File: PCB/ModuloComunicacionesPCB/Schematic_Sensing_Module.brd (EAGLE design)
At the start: 160 x 100 mm, 73 parts, among them J1 TERMINAL-TB3, J2 TERMINAL-TB3, J3 TERMINAL-TB3, J4 TERMINAL-TB3, Q1 CSM-7X-DU, Q2 MMBT2222A, SW2 1825910-6, U1 ATMEGA328P-PU, U2 LP38692MP-5.0, U3 MCP1501T-18E/SN, U4 ACS723LLCTR-05AB-T, U5 OPA320AIDBVR

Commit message: avances en placing de la pcb del transmisor
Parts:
- removed BAT_PIN: (no value), pinhead:1X02
- removed C24: (no value), rcl:C0805
- removed FTDI_PIN: (no value), pinhead:1X04
- removed J1, J2, J3, J4: TERMINAL-TB3, TERMINAL-TB001:TERMINAL-TB3
- removed Q2: MMBT2222A, MMBT2222A:SOT23
- removed R15, R16, R17, R3, R4, R5: 0.1, rcl:R1206
- removed U$2, U$7: REF3450, SOT95P280X145-6N:SOT95P280X145-6N
- removed U$3: MCP6002-E/MS, MCP6002-E_MS:SOP65P490X110-8N
- removed U$6: TERMINAL-TB2, TERMINAL-TB001:TERMINAL-TB2
- removed U2: LP38692MP-5.0, LP38692MP-5.0:SOT150P696X180-5N
- removed U4: ACS723LLCTR-05AB-T, ACS723LLCTR-05AB-T:SOIC127P600X175-8N
- removed U5: OPA320AIDBVR, OPA320AIDBVR:SOT95P280X145-5N
- added 2N2222: MMBT2222A, MMBT2222A:SOT23
- added ACS723: ACS723LLCTR-05AB-T, ACS723LLCTR-05AB-T:SOIC127P600X175-8N
- added C29, C30, C31, C32: 0.1uF, rcl:C1206
- added C33: 1nF, rcl:C1206
- added C34, C35: 2.2uF, rcl:C1206
- added IACT: (no value), TERMINAL-TB001:TERMINAL-TB2
- added JP1: (no value), pinhead:1X04/90
- added LP38692: LP38692MP-5.0, LP38692MP-5.0:SOT150P696X180-5N
- added MCP6002: MCP6002-E/MS, MCP6002-E_MS:SOP65P490X110-8N
- added OPA320: OPA320AIDBVR, OPA320AIDBVR:SOT95P280X145-5N
- added R3450, REF3450: REF3450, SOT95P280X145-6N:SOT95P280X145-6N
- added TS1, TS2, WS1, WS2: (no value), TERMINAL-TB001:TERMINAL-TB3
- C11, C12: value 22p -> 22pF; device rcl:C1206 -> rcl:C0805
- C14, C15, C20, C21: value 100n -> 100nF
- C17: value 8.2pF -> 18pF
- C2, C3: value 1uF -> cambiar por los de 10uF ceramicos de didacticas
- C22: value 0.1u -> 0.1uF
- C25, C26, C27, C28: value 0.1nF -> 0.1uF
- U$4: value INA219_BB -> INABB; device INA219_BB:INA219_BB -> INA219BB:INA219-MODULE
- moved C27 315.3 mm to (98.1, 114.0)
- moved C28 309.0 mm to (80.7, 116.0)
- moved C22 235.1 mm to (151.1, 114.0)
- moved C25 210.0 mm to (60.2, 23.8), turned to 180 degrees
- moved U$8 208.7 mm to (83.3, 59.1), turned to 270 degrees
- moved R19 205.8 mm to (60.1, 18.4), turned to 180 degrees
- moved LED4 199.4 mm to (115.7, 74.0), turned to 90 degrees
- moved C26 196.9 mm to (46.2, 17.6), turned to 270 degrees
- moved LED3 195.6 mm to (116.1, 66.9), turned to 270 degrees
- moved R1 192.7 mm to (90.5, 38.5), turned to 180 degrees
- moved R12 191.1 mm to (98.1, 106.3)
- moved R7 189.3 mm to (107.7, 67.0), turned to 180 degrees
- moved SW2 187.5 mm to (115.8, 57.7), turned to 90 degrees
- moved R18 186.2 mm to (41.4, 17.6), turned to 270 degrees
- moved C23 170.4 mm to (66.0, 38.5)
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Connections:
- removed net +5V: U$1.IN+
- removed net A0: U1.23
- removed net A1: U1.24
- removed net A2: U1.25
- removed net A3: U1.26
- removed net N$1: R3.2, U$2.1
- removed net N$10: U$6.1, U4.1, U4.2
- removed net N$11: U$6.2, U4.3, U4.4
- removed net N$12: R11.2, U4.7
- removed net N$13: C9.1, R12.2, U5.3
- removed net N$15: C10.1, R13.1, U5.1, U5.4
- removed net N$18: R16.2, U$7.6
- removed net N$19: R17.2, U$7.5
- removed net N$20: R15.2, U$7.1
- removed net N$24: C25.1, R19.1, U$3.3
- removed net N$25: C26.1, R18.1, U$3.5
- removed net N$5: R4.2, U$2.6
- removed net N$6: R5.2, U$2.5
- removed net N$8: R10.1, U4.6
- removed net VOUT-: U$1.VOUT-
- new net BWSEL: ACS723.6, R10.1
- new net IP+: ACS723.1, ACS723.2, IACT.1
- new net IP-: ACS723.3, ACS723.4, IACT.2
- new net VIN+: C9.1, OPA320.3, R12.2
- new net VIN-: C10.1, OPA320.1, OPA320.4, R13.1
- new net VO: ACS723.7, C33.1, R11.2
- net B+INA: now also U$4.6
- net B-INA: now also U$4.5; no longer BAT_PIN.1
- net BATL: now also U1.13; no longer U1.11
- net DATAT1: now also TS1.2, U1.14; no longer J3.2
- net DATAT2: now also TS2.2, U1.15; no longer J4.2
- net DATAW1: now also C25.1, MCP6002.3, R19.1, WS1.3; no longer J1.3
- net DATAW2: now also C26.1, MCP6002.5, R18.1, WS2.3; no longer J2.3
- net DTR: now also JP1.4; no longer FTDI_PIN.4
- net GND: now also ACS723.5, C29.2, C30.2, C31.2, C32.2, C33.2, C34.1, C35.2, JP1.1, LP38692.5, MCP6002.4, OPA320.2, R3450.1, R3450.2, REF3450.1, REF3450.2, TS1.3, TS2.3, U$1.VOUT-, U$4.2, U$8.DIO0, U$8.DIO1, U$8.DIO2, U$8.DIO3, U$8.DIO4, U1.25, U1.26, U1.6, WS1.1, WS2.1; no longer BAT_PIN.2, C24.2, FTDI_PIN.1, J1.1, J2.1, J3.3, J4.3, R15.1, R3.1, U$2.2, U$3.4, U$7.2, U2.5, U4.5, U5.2
- net N$2: now also 2N2222.1; no longer Q2.1
- net OSC+: now also C12.1; no longer C11.1
- net OSC-: now also C11.1; no longer C12.1
- net RX0: now also JP1.3; no longer FTDI_PIN.3
- net RX1: now also U$8.TX
- net SCL: now also U$4.3
- net SDA: now also U$4.4
- net TX0: now also JP1.2; no longer FTDI_PIN.2
- net TX1: now also U$8.RX
- net VACS: now also ACS723.8, REF3450.5, REF3450.6; no longer R16.1, R17.1, U4.8
- net VDD33: now also C29.1, U$4.1; no longer C17.1, C24.1
- net VLP5: now also C30.1, C31.1, C32.1, C34.2, LP38692.3, MCP6002.8, TS1.1, TS2.1, U1.21, WS1.2, WS2.2; no longer J1.2, J2.2, J3.1, J4.1, U$3.8, U2.3
- net VOREG: now also 2N2222.2, R3450.3, R3450.4, REF3450.3, REF3450.4; no longer Q2.2, U$2.3, U$2.4, U$7.3, U$7.4
- net VOUT+: now also C17.1, C35.1
- net VOW1: now also MCP6002.1, MCP6002.2, U1.23; no longer U$3.1, U$3.2
- net VOW2: now also MCP6002.6, MCP6002.7, U1.24; no longer U$3.6, U$3.7
- net VREF5: now also OPA320.5, R3450.5, R3450.6; no longer R4.1, R5.1, U5.5
- net VSUPPLY: now also 2N2222.3, LP38692.1, LP38692.4; no longer Q2.3, U2.1, U2.4

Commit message: placing almost done
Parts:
- removed C34: 2.2uF, rcl:C1206
- removed JP1: (no value), pinhead:1X04/90
- removed LED3, LED4: (no value), led:CHIPLED_1206
- removed U$4: INABB, INA219BB:INA219-MODULE
- removed U$5: MCP33121, mcp33121:MSOP10
- removed U1: ATMEGA328P-PU, Atmel_By_element14_Batch_1-00:DIP254P762X457-28
- removed U3: MCP1501T-18E/SN, MCP1501T-18E_SN:SOIC127P600X175-8N
- added ATMEGA328P: ATMEGA328P-PU, Atmel_By_element14_Batch_1-00:DIP254P762X457-28
- added BAT+, BAT-: (no value), led:CHIPLED_1206
- added INA219: INABB, INA219BB:INA219-MODULE
- added JP2: (no value), pinhead:1X04
- added MCP18: MCP1501T-18E/SN, MCP1501T-18E_SN:SOIC127P600X175-8N
- added MCP33121: MCP33121, mcp33121:MSOP10
- added TS3: (no value), TERMINAL-TB001:TERMINAL-TB3
- C18: value 1uF -> 0.1uF
- C19: value 10uF -> 0.1uF
- moved R9 144.9 mm to (28.8, 12.7)
- moved R6 126.5 mm to (28.6, 20.9)
- moved C32 125.6 mm to (129.2, 24.3), turned to 180 degrees
- moved R11 118.6 mm to (111.6, 40.0)
- moved R14 117.9 mm to (99.1, 44.0), turned to 180 degrees
- moved R13 115.0 mm to (99.5, 40.2), turned to 180 degrees
- moved C20 112.0 mm to (92.6, 32.6), turned to 180 degrees
- moved C8 112.0 mm to (28.9, 16.9)
- moved C16 111.4 mm to (99.2, 32.7)
- moved C19 107.0 mm to (84.2, 24.5), turned to 180 degrees
- moved C31 105.3 mm to (106.1, 24.6), turned to 180 degrees
- moved C7 104.8 mm to (20.0, 22.6)
- moved C15 103.6 mm to (116.1, 32.1), turned to 270 degrees
- moved C21 102.2 mm to (92.5, 44.1)
- moved IACT 101.3 mm to (129.0, 38.4), turned to 90 degrees
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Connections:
- removed net N$16: C13.2, R13.2, U$5.3
- removed net N$17: C13.1, R14.2, U$5.4
- removed net N$7: R6.2, R9.2, U3.7, U3.8
- new net DATAT3: ATMEGA328P.13, C18.1, TS3.2
- new net IN+: C13.2, MCP33121.3, R13.2
- new net IN-: C13.1, MCP33121.4, R14.2
- new net VOMCP18: MCP18.7, MCP18.8, R6.2, R9.2
- net AMISO: now also ATMEGA328P.18, MCP33121.7; no longer U$5.7, U1.18
- net AMOSI: now also ATMEGA328P.17, MCP33121.9; no longer U$5.9, U1.17
- net ASCK: now also ATMEGA328P.19, MCP33121.8; no longer U$5.8, U1.19
- net ASS: now also ATMEGA328P.16, MCP33121.6; no longer U$5.6, U1.16
- net B+INA: now also INA219.6; no longer U$4.6
- net B-INA: now also INA219.5; no longer U$4.5
- net BATH: now also ATMEGA328P.11; no longer U1.12
- net BATL: now also ATMEGA328P.12; no longer U1.13
- net DATAT1: now also ATMEGA328P.14; no longer U1.14
- net DATAT2: now also ATMEGA328P.15; no longer U1.15
- net DTR: now also JP2.4; no longer JP1.4
- net GND: now also ATMEGA328P.22, ATMEGA328P.25, ATMEGA328P.26, ATMEGA328P.6, ATMEGA328P.8, BAT+.C, BAT-.C, C19.2, INA219.2, JP2.1, MCP18.2, MCP18.4, MCP18.5, MCP18.6, MCP33121.5, TS1.1, TS2.1, TS3.1; no longer C19.1, C34.1, JP1.1, LED3.C, LED4.C, TS1.3, TS2.3, U$4.2, U$5.5, U1.22, U1.25, U1.26, U1.6, U1.8, U3.2, U3.4, U3.5, U3.6
- net N$3: now also BAT-.A; no longer LED3.A
- net N$4: now also BAT+.A; no longer LED4.A
- net OSC+: now also ATMEGA328P.9; no longer U1.9
- net OSC-: now also ATMEGA328P.10; no longer U1.10
- net RST: now also ATMEGA328P.1; no longer U1.1
- net RX0: now also ATMEGA328P.2, JP2.3; no longer JP1.3, U1.2
- net RX1: now also ATMEGA328P.4; no longer U1.4
- net SCL: now also ATMEGA328P.28, INA219.3; no longer U$4.3, U1.28
- net SDA: now also ATMEGA328P.27, INA219.4; no longer U$4.4, U1.27
- net TX0: now also ATMEGA328P.3, JP2.2; no longer JP1.2, U1.3
- net TX1: now also ATMEGA328P.5; no longer U1.5
- net VDD33: now also INA219.1; no longer U$4.1
- net VLP5: now also ATMEGA328P.20, ATMEGA328P.21, ATMEGA328P.7, C19.1, MCP33121.10, TS1.3, TS2.3, TS3.3; no longer C19.2, C34.2, TS1.1, TS2.1, U$5.10, U1.20, U1.21, U1.7
- net VOW1: now also ATMEGA328P.23; no longer U1.23
- net VOW2: now also ATMEGA328P.24; no longer U1.24
- net VREF18: now also MCP33121.2; no longer U$5.2
- net VREF5: now also MCP18.1, MCP18.3, MCP33121.1; no longer C18.1, U$5.1, U3.1, U3.3

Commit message: Finished Placing-Give a review
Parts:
- C2, C3: value cambiar por los de 10uF ceramicos de didacticas -> 10uF
- C23, C6: value 1u -> 10u
- moved MCP18 58.4 mm to (54.2, 64.5)
- moved C8 57.1 mm to (60.4, 64.6), turned to 270 degrees
- moved R6 55.7 mm to (63.4, 64.4), turned to 270 degrees
- moved R9 52.8 mm to (54.2, 58.9), turned to 180 degrees
- moved C7 50.1 mm to (47.6, 64.5), turned to 270 degrees
- moved LP38692 43.0 mm to (15.8, 46.9)
- moved C17 41.1 mm to (9.84, 37.7)
- moved C3 37.8 mm to (22.9, 46.3), turned to 90 degrees
- moved C35 36.3 mm to (15.8, 37.8)
- moved D1 30.5 mm to (45.4, 71.6)
- moved JP2 29.4 mm to (53.8, 76.5)
- moved ATMEGA328P 29.4 mm to (57.8, 22.3)
- moved C12 29.2 mm to (46.4, 36.0)
- moved Q1 29.2 mm to (42.0, 33.9)
- moved C11 29.2 mm to (46.4, 31.3)
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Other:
- board size 160 x 100 mm -> 109 x 82 mm

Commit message: pcb ruteada falta plano de tierra
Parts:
- removed JP2: (no value), pinhead:1X04
- removed ON_OFF: (no value), pinhead:1X03
- removed SW2: 1825910-6, button1825910-6:SW_1825910-6-4
- removed TS1, TS2, TS3: (no value), TERMINAL-TB001:TERMINAL-TB3
- removed U$1: MODULO_CARGA_DEVICE, Modulo_Carga:MODULO_CARGA
- added BATPIN: (no value), pinhead:1X02
- added FTDI: (no value), pinhead:1X04
- added JP1, ON/OFF: (no value), pinhead:1X03
- added POWER-SUPP: MODULO_CARGA_DEVICE, Modulo_Carga:MODULO_CARGA
- added RESET: 1825910-6, button1825910-6:SW_1825910-6-4
- added T1, T2, T3: (no value), TERMINAL-TB001:TERMINAL-TB3
- moved BAT- 75.7 mm to (42.9, 4.19), turned to 180 degrees
- moved BAT+ 75.1 mm to (37.8, 5.21), turned to 180 degrees
- moved R7 69.6 mm to (43.0, 11.9)
- moved R8 66.8 mm to (37.9, 11.8), turned to 90 degrees
- moved C29 23.4 mm to (67.7, 58.4), turned to 0 degrees
- moved C21 20.1 mm to (60.2, 18.8), flipped to the bottom, turned to 90 degrees
- moved R14 19.0 mm to (66.9, 19.8)
- moved C2 16.5 mm to (31.8, 52.2)
- moved C23 16.3 mm to (38.8, 64.5)
- moved LP38692 16.0 mm to (31.8, 46.9)
- moved C3 15.9 mm to (38.8, 46.2), turned to 270 degrees
- moved C1 15.8 mm to (45.7, 69.3)
- moved D1 15.2 mm to (60.6, 71.8), turned to 90 degrees
- moved R2 15.0 mm to (38.2, 69.5), turned to 180 degrees
- moved C4 13.4 mm to (22.3, 65.4), turned to 0 degrees
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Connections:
- net N$2 renamed BASE
- removed net AMOSI: ATMEGA328P.17, MCP33121.9
- removed net VO: ACS723.7, C33.1, R11.2
- new net VIN: C33.1, JP1.2, R11.2
- new net VOACS: ACS723.7, JP1.1
- net B+INA: now also POWER-SUPP.BAT+; no longer U$1.BAT+
- net B-INA: now also BATPIN.1
- net DATAT1: now also ATMEGA328P.15, T1.2; no longer ATMEGA328P.14, TS1.2
- net DATAT2: now also ATMEGA328P.13, T2.2; no longer ATMEGA328P.15, TS2.2
- net DATAT3: now also ATMEGA328P.14, T3.2; no longer ATMEGA328P.13, TS3.2
- net DATAW1: now also WS1.2; no longer WS1.3
- net DATAW2: now also WS2.2; no longer WS2.3
- net DTR: now also FTDI.4; no longer JP2.4
- net GND: now also ATMEGA328P.17, BATPIN.2, FTDI.1, JP1.3, POWER-SUPP.BAT-, POWER-SUPP.IN-, POWER-SUPP.VOUT-, RESET.1, RESET.2, T1.1, T2.1, T3.1; no longer JP2.1, SW2.1, SW2.2, TS1.1, TS2.1, TS3.1, U$1.BAT-, U$1.IN-, U$1.VOUT-
- net RST: now also RESET.3, RESET.4; no longer SW2.3, SW2.4
- net RX0: now also FTDI.3; no longer JP2.3
- net TX0: now also FTDI.2; no longer JP2.2
- net VLP5: now also MCP33121.9, T1.3, T2.3, T3.3, WS1.3, WS2.3; no longer ATMEGA328P.21, TS1.3, TS2.3, TS3.3, WS1.2, WS2.2
- net VOUT+: now also ON/OFF.3, POWER-SUPP.VOUT+; no longer C17.1, C35.1, ON_OFF.3, U$1.VOUT+
- net VOW1: now also ATMEGA328P.24; no longer ATMEGA328P.23
- net VOW2: now also ATMEGA328P.23; no longer ATMEGA328P.24
- net VSUPPLY: now also C17.1, C35.1, ON/OFF.2, U$8.5V; no longer ON_OFF.2
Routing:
- net GND: track 0.00 -> 1286.8 mm, vias 0 -> 48
- net VLP5: track 0.00 -> 346.7 mm, vias 0 -> 7
- net VREF5: track 0.00 -> 121.0 mm, vias 0 -> 2
- net VACS: track 0.00 -> 104.3 mm, vias 0 -> 3
- net VSUPPLY: track 0.00 -> 96.5 mm, vias 0 -> 4
- net VDD33: track 0.00 -> 92.6 mm, vias 0 -> 2
- net RST: track 0.00 -> 60.7 mm, vias 0 -> 1
- net B+INA: track 0.00 -> 60.1 mm
- net VREF18: track 0.00 -> 55.1 mm, vias 0 -> 1
- net TX1: track 0.00 -> 52.0 mm
- net RX1: track 0.00 -> 50.8 mm
- net DATAT1: track 0.00 -> 48.5 mm, vias 0 -> 1
- net DATAW1: track 0.00 -> 44.1 mm
- net IP+: track 0.00 -> 36.9 mm, vias 0 -> 4
- net DATAW2: track 0.00 -> 36.6 mm
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- added copper zone on layer 1, net IP+
- added copper zone on layer 1, net IP-
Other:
- board size 109 x 82 mm -> 101.8 x 76 mm
- board text added: "+"
- board text added: "-"
- board text added: "CSENSOR"
- board text added: "DTR"
- board text added: "GND"
- board text added: "RX"
- board text added: "TX"
- board text added: "VIN"
- board text added: "XBEE"
- board text added: "ecotic"

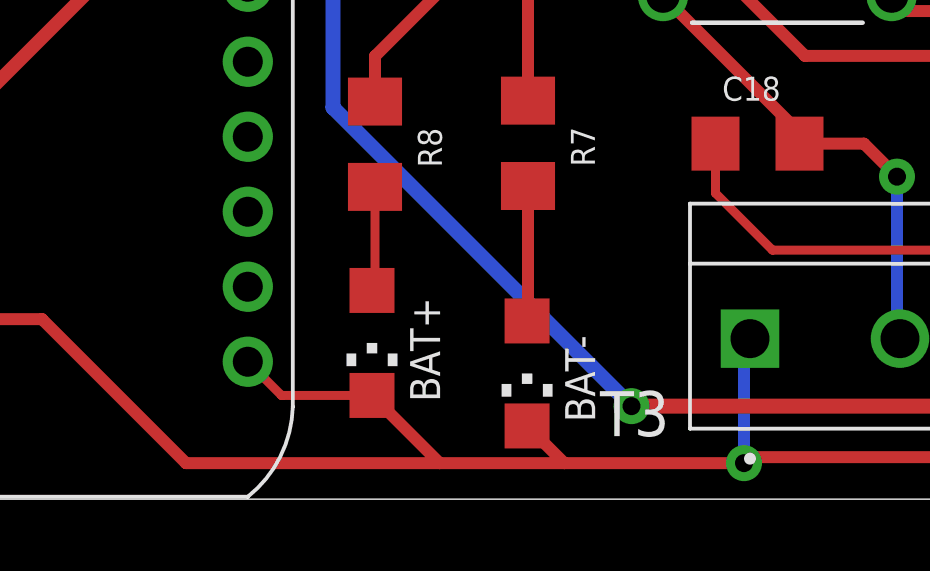
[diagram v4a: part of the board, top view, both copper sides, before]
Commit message: modelado 3D terminado falta plano de tierra
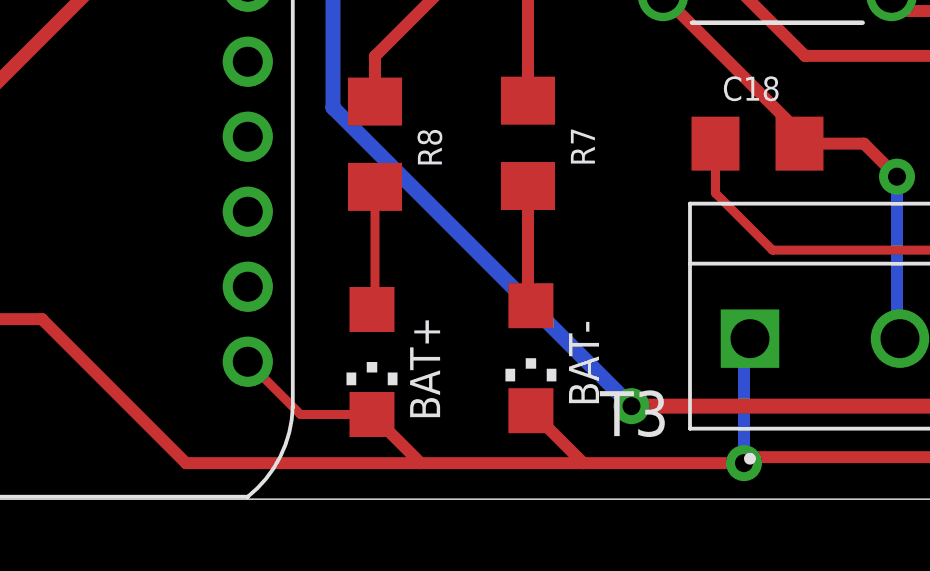
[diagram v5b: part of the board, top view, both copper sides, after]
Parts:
- moved BAT+ 0.64 mm to (37.8, 4.57)
- moved BAT- 0.52 mm to (43.0, 4.70)
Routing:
- net N$4: track 3.49 -> 4.13 mm
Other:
- board text removed: "ecotic"

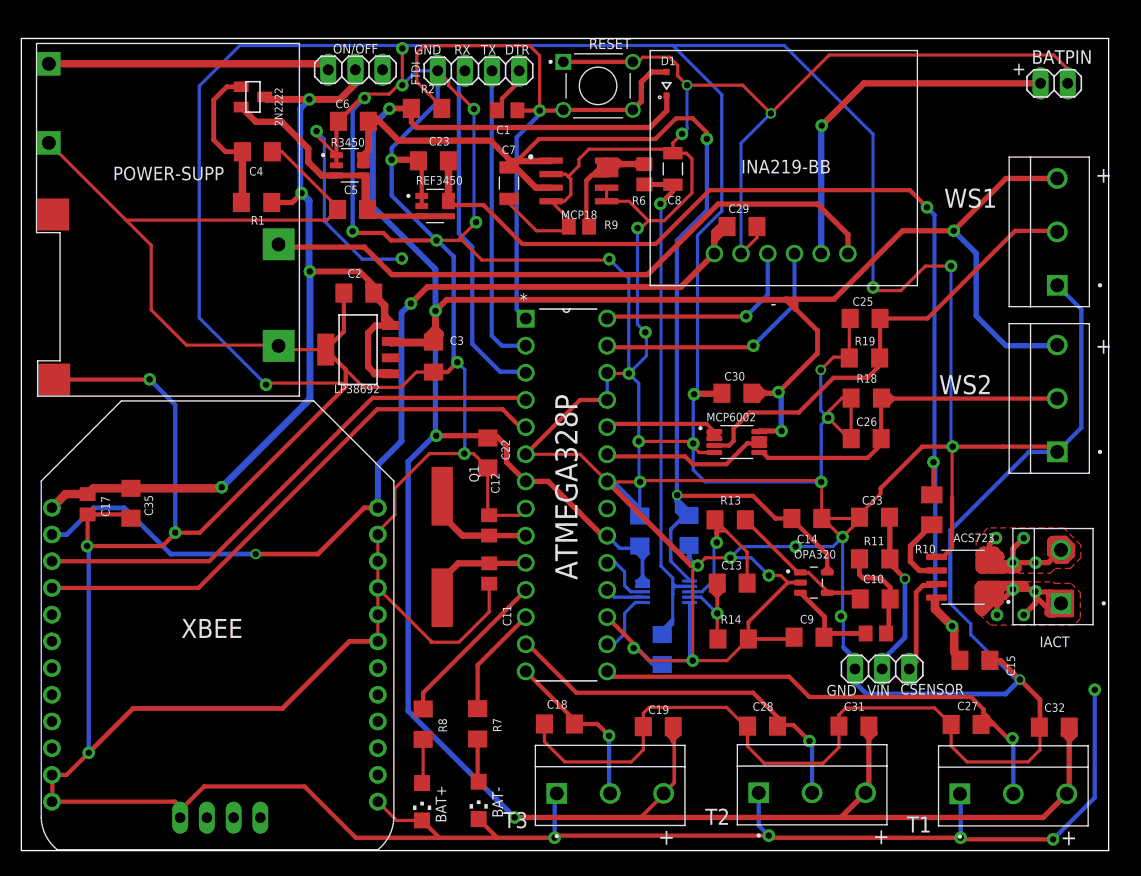
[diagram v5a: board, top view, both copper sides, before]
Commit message: ajustando tierra
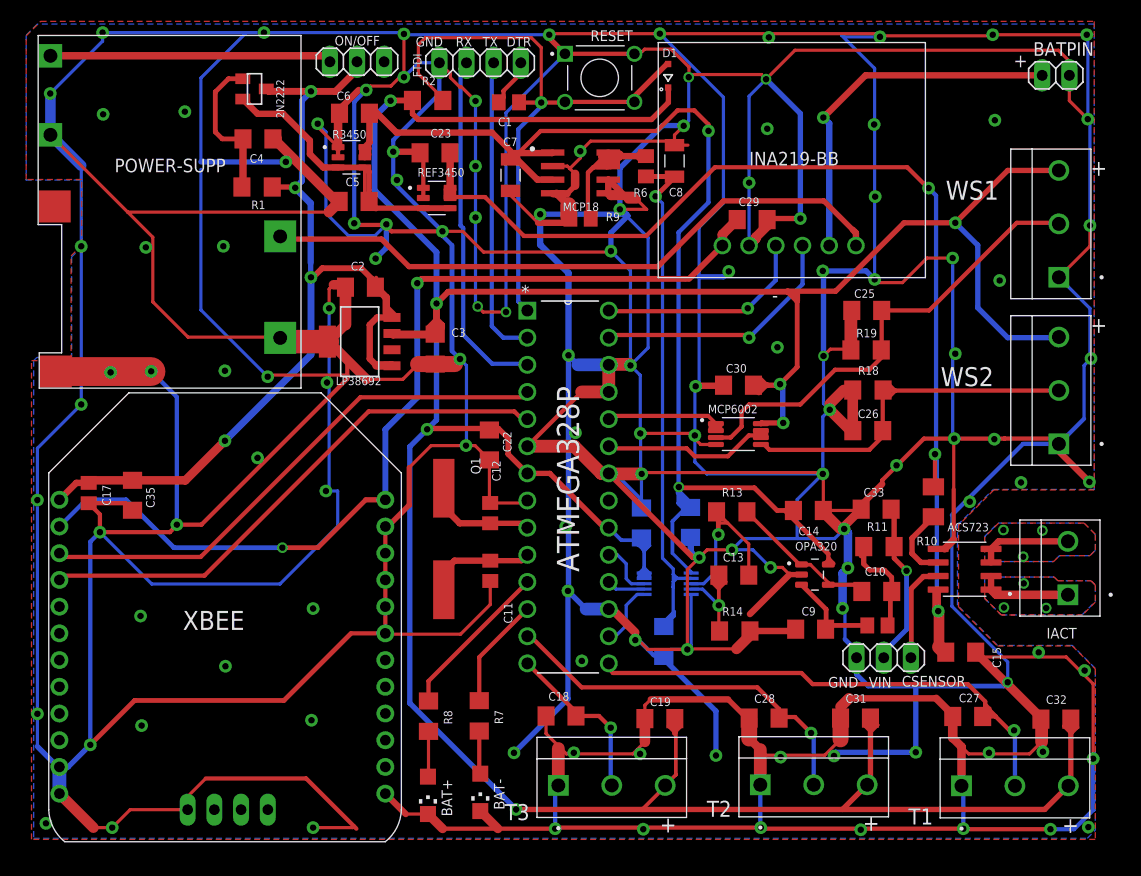
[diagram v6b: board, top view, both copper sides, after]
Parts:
- moved C15 1.53 mm to (88.2, 18.6)
- moved R1 1.45 mm to (22.3, 62.1)
- moved R11 1.22 mm to (80.5, 28.4)
- moved C4 1.20 mm to (22.4, 66.6)
- moved C12 1.15 mm to (44.1, 31.6)
- moved C29 1.15 mm to (68.6, 59.0)
- moved INA219 1.06 mm to (72.3, 64.6)
- moved JP1 1.06 mm to (81.0, 18.1)
- moved C17 1.05 mm to (6.55, 33.5)
- moved IACT 1.03 mm to (98.2, 26.4)
- moved U$8 1.03 mm to (19.3, 21.8)
- moved R8 0.90 mm to (38.4, 12.6)
- moved BAT+ 0.81 mm to (38.3, 5.17)
- moved R6 0.76 mm to (58.7, 64.0)
- moved C8 0.76 mm to (61.4, 64.5)
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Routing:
- net GND: track 1286.9 -> 1706.7 mm, vias 48 -> 124
- net IP+: track 36.9 -> 8.67 mm, vias 4 -> 3
- net IP-: track 29.2 -> 8.76 mm, vias 4 -> 3
- net VSUPPLY: track 96.5 -> 90.9 mm
- net VDD33: track 92.6 -> 89.8 mm
- net IN+: track 16.5 -> 18.0 mm
- net TX1: track 52.0 -> 50.6 mm
- net VLP5: track 346.7 -> 345.5 mm
- net DATAT2: track 35.8 -> 36.8 mm
- net VREF18: track 55.1 -> 56.1 mm
- net RST: track 60.7 -> 59.9 mm
- net B-INA: track 34.1 -> 34.7 mm
- net BASE: track 14.8 -> 14.2 mm
- net TX0: track 32.4 -> 33.0 mm
- added copper zone on layer 1, net GND
- added copper zone on layer 16, net GND
- added copper zone on layer 16, net IP+
- added copper zone on layer 16, net IP-
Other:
- board outline removed

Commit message: transmisor terminado
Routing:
- net GND: track 1706.7 -> 1959.7 mm, vias 124 -> 126
- net VLP5: track 345.5 -> 324.0 mm
- net VOMCP18: track 23.8 -> 19.0 mm
- net IN-: track 13.2 -> 8.48 mm
- net VREF18: track 56.1 -> 53.3 mm
- net IN+: track 18.0 -> 15.5 mm
- net VSUPPLY: track 90.9 -> 89.2 mm
- net DATAT1: track 48.8 -> 47.2 mm
- net N$14: track 10.9 -> 9.43 mm
- net VREF5: track 121.2 -> 119.8 mm
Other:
- board outline added: 101.7 x 77.8 mm
